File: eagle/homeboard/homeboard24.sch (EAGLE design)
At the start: 128 parts, among them IC1 XCF02S, IC2 25LC080SN, IC3 ATMEGA32U2-TQFP, Q5 BC848SMD, Q6 BC848SMD, Q7 BC848SMD, Q8 BC848SMD, T1 BSS138, T2 BC848, T3 BSS138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

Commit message: added text
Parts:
- removed C28, C30, C31: 100nF, rcl:C-EUC0603
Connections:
- net GND: no longer C28.2, C30.2, C31.2
- net VCC: no longer C28.1, C30.1, C31.1
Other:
- note added: "atmel"
- note added: "bot right"
- note added: "flash"
- note added: "prom"
- note added: "ram"
- moved on the sheet: C29, C32, C34

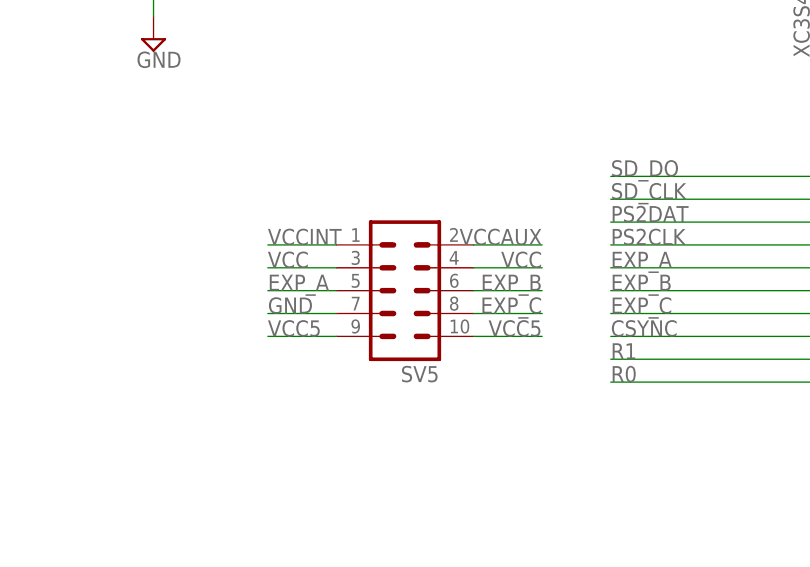
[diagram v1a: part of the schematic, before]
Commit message: moved ps2 stuff to top layer
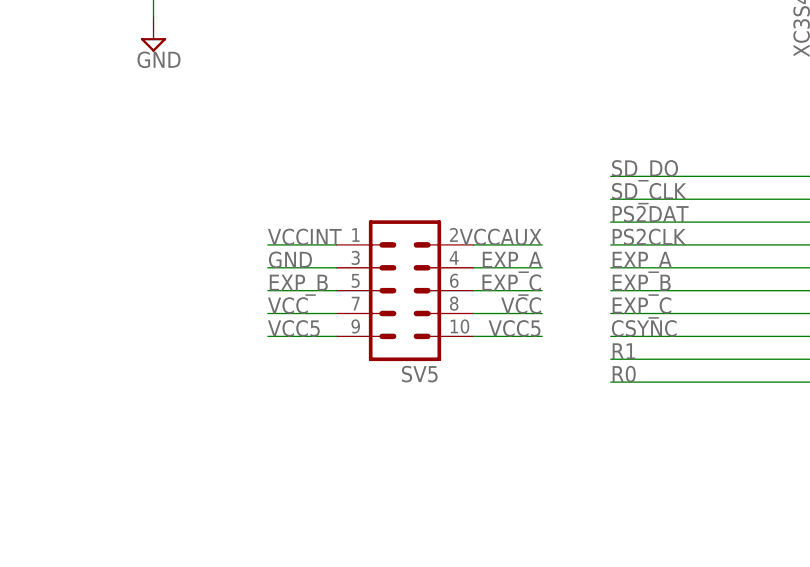
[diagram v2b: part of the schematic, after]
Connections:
- net EXP_A: now also SV5.4; no longer SV5.5
- net EXP_B: now also SV5.5; no longer SV5.6
- net EXP_C: now also SV5.6; no longer SV5.8
- net GND: now also SV5.3; no longer SV5.7
- net VCC: now also SV5.7, SV5.8; no longer SV5.3, SV5.4
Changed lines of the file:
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@@
-</segment>
-<segment>
-<pinref part="SV5" gate="G$1" pin="7"/>
-<wire x1="60.96" y1="-73.66" x2="68.58" y2="-73.66" width="0.1524" layer="91"/>
-<label x="60.96" y="-73.66" size="1.778" layer="95"/>
 </segment>
 <segment>
@@
 <pinref part="SV2" gate="1" pin="2"/>
 <wire x1="292.1" y1="-35.56" x2="292.1" y2="-25.4" width="0.1524" layer="91"/>
+</segment>
+<segment>
+<pinref part="SV5" gate="G$1" pin="3"/>
+<wire x1="60.96" y1="-68.58" x2="68.58" y2="-68.58" width="0.1524" layer="91"/>
+<label x="60.96" y="-68.58" size="1.778" layer="95"/>
 </segment>
 </net>
@@
 </segment>
 <segment>
-<pinref part="SV5" gate="G$1" pin="3"/>
-<wire x1="60.96" y1="-68.58" x2="68.58" y2="-68.58" width="0.1524" layer="91"/>
-<label x="60.96" y="-68.58" size="1.778" layer="95"/>
-</segment>
-<segment>
-<pinref part="SV5" gate="G$1" pin="4"/>
-<wire x1="91.44" y1="-68.58" x2="83.82" y2="-68.58" width="0.1524" layer="91"/>
-<label x="91.44" y="-68.58" size="1.778" layer="95" rot="MR0"/>
-</segment>
-<segment>
 <pinref part="R55" gate="G$1" pin="1"/>
 <pinref part="R56" gate="G$1" pin="1"/>
@@
 <junction x="287.02" y="-33.02"/>
 <label x="266.7" y="-33.02" size="1.778" layer="95"/>
+</segment>
+<segment>
+<pinref part="SV5" gate="G$1" pin="7"/>
+<wire x1="60.96" y1="-73.66" x2="68.58" y2="-73.66" width="0.1524" layer="91"/>
+<label x="60.96" y="-73.66" size="1.778" layer="95"/>
+</segment>
+<segment>
+<pinref part="SV5" gate="G$1" pin="8"/>
+<wire x1="91.44" y1="-73.66" x2="83.82" y2="-73.66" width="0.1524" layer="91"/>
+<label x="91.44" y="-73.66" size="1.778" layer="95" rot="MR0"/>
 </segment>
 </net>
@@
 </segment>
 <segment>
-<pinref part="SV5" gate="G$1" pin="5"/>
-<wire x1="60.96" y1="-71.12" x2="68.58" y2="-71.12" width="0.1524" layer="91"/>
-<label x="60.96" y="-71.12" size="1.778" layer="95"/>
+<pinref part="SV5" gate="G$1" pin="4"/>
+<wire x1="91.44" y1="-68.58" x2="83.82" y2="-68.58" width="0.1524" layer="91"/>
+<label x="91.44" y="-68.58" size="1.778" layer="95" rot="MR0"/>
 </segment>
 </net>
@@
 </segment>
 <segment>
-<pinref part="SV5" gate="G$1" pin="6"/>
-<wire x1="91.44" y1="-71.12" x2="83.82" y2="-71.12" width="0.1524" layer="91"/>
-<label x="91.44" y="-71.12" size="1.778" layer="95" rot="MR0"/>
+<pinref part="SV5" gate="G$1" pin="5"/>
+<wire x1="60.96" y1="-71.12" x2="68.58" y2="-71.12" width="0.1524" layer="91"/>
+<label x="60.96" y="-71.12" size="1.778" layer="95"/>
 </segment>
 </net>
@@
 </segment>
 <segment>
-<pinref part="SV5" gate="G$1" pin="8"/>
-<wire x1="91.44" y1="-73.66" x2="83.82" y2="-73.66" width="0.1524" layer="91"/>
-<label x="91.44" y="-73.66" size="1.778" layer="95" rot="MR0"/>
-</segment>
-</net>
+<pinref part="SV5" gate="G$1" pin="6"/>
+<wire x1="91.44" y1="-71.12" x2="83.82" y2="-71.12" width="0.1524" layer="91"/>
+<label x="91.44" y="-71.12" size="1.778" layer="95" rot="MR0"/>
+</segment>
+</net>

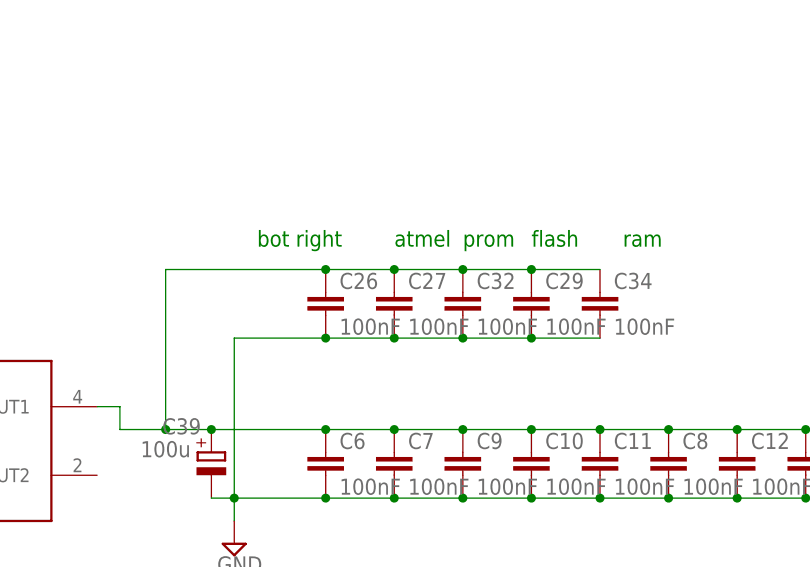
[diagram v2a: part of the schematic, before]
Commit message: removed spare cap
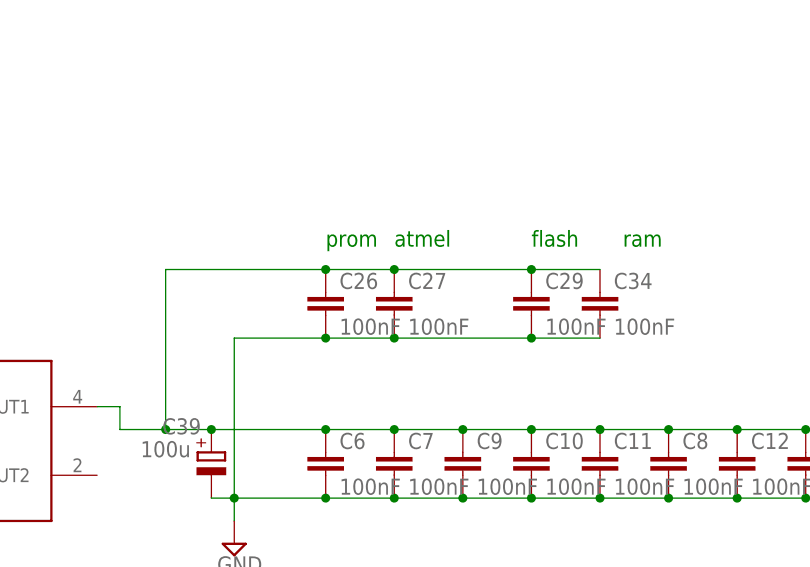
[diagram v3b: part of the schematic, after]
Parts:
- removed C32: 100nF, rcl:C-EUC0603
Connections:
- net GND: no longer C32.2
- net VCC: no longer C32.1
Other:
- note removed: "bot right"
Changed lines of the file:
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@@
 <part name="C27" library="rcl" deviceset="C-EU" device="C0603" value="100nF"/>
 <part name="C29" library="rcl" deviceset="C-EU" device="C0603" value="100nF"/>
-<part name="C32" library="rcl" deviceset="C-EU" device="C0603" value="100nF"/>
 <part name="X6" library="con-cypressindustries" deviceset="MINI-USB_4P-" device="85-32004-10X"/>
 <part name="R53" library="rcl" deviceset="R-EU_" device="R0805" value="22"/>
@@
 <text x="271.78" y="-254" size="1.778" layer="91">Possible alternative:</text>
 <text x="-139.7" y="132.08" size="1.778" layer="91">atmel</text>
-<text x="-154.94" y="132.08" size="1.778" layer="91">bot right</text>
-<text x="-132.08" y="132.08" size="1.778" layer="91">prom</text>
+<text x="-147.32" y="132.08" size="1.778" layer="91">prom</text>
 <text x="-124.46" y="132.08" size="1.778" layer="91">flash</text>
 <text x="-114.3" y="132.08" size="1.778" layer="91">ram</text>
@@
 <instance part="C27" gate="G$1" x="-139.7" y="127"/>
 <instance part="C29" gate="G$1" x="-124.46" y="127"/>
-<instance part="C32" gate="G$1" x="-132.08" y="127"/>
 <instance part="X6" gate="G$1" x="358.14" y="119.38" rot="MR0"/>
 <instance part="R53" gate="G$1" x="375.92" y="121.92" rot="MR180"/>
@@
 <junction x="-147.32" y="121.92"/>
 <junction x="-139.7" y="121.92"/>
-<pinref part="C32" gate="G$1" pin="2"/>
-<wire x1="-139.7" y1="121.92" x2="-132.08" y2="121.92" width="0.1524" layer="91"/>
 <pinref part="C29" gate="G$1" pin="2"/>
-<wire x1="-132.08" y1="121.92" x2="-124.46" y2="121.92" width="0.1524" layer="91"/>
-<junction x="-132.08" y="121.92"/>
+<wire x1="-139.7" y1="121.92" x2="-124.46" y2="121.92" width="0.1524" layer="91"/>
 <wire x1="-157.48" y1="121.92" x2="-157.48" y2="104.14" width="0.1524" layer="91"/>
 <junction x="-157.48" y="104.14"/>
@@
 <junction x="-147.32" y="129.54"/>
 <junction x="-139.7" y="129.54"/>
-<pinref part="C32" gate="G$1" pin="1"/>
-<wire x1="-139.7" y1="129.54" x2="-132.08" y2="129.54" width="0.1524" layer="91"/>
 <pinref part="C29" gate="G$1" pin="1"/>
-<wire x1="-132.08" y1="129.54" x2="-124.46" y2="129.54" width="0.1524" layer="91"/>
-<junction x="-132.08" y="129.54"/>
+<wire x1="-139.7" y1="129.54" x2="-124.46" y2="129.54" width="0.1524" layer="91"/>
 <pinref part="U$4" gate="G$1" pin="VOUT1"/>
 <wire x1="-172.72" y1="114.3" x2="-170.18" y2="114.3" width="0.1524" layer="91"/>

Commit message: moving around
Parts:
- removed SV4: (no value), con-lstb:MA10-2
- added SV1: (no value), con-lstb:MA10-2
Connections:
- net AT_RESET: now also SV1.2; no longer SV4.1
- net EMER_BOOT: now also SV1.1; no longer SV4.2
- net GND: now also SV1.5, SV1.6; no longer SV4.3, SV4.4
- net HDR_MISO: now also SV1.15; no longer SV4.13
- net HDR_MOSI: now also SV1.19; no longer SV4.17
- net HDR_SCLK: now also SV1.17; no longer SV4.15
- net HDR_SEL: now also SV1.13; no longer SV4.11
- net HDR_SPARE: now also SV1.11; no longer SV4.9
- net SPI_MISO: now also SV1.16; no longer SV4.14
- net SPI_MOSI: now also SV1.20; no longer SV4.18
- net SPI_SCLK: now also SV1.18; no longer SV4.16
- net SPI_SEL: now also SV1.14; no longer SV4.12
- net TCK: now also SV1.9; no longer SV4.7
- net TDI_FPGA: now also SV1.7; no longer SV4.5
- net TDO_EXP: now also SV1.8; no longer SV4.6
- net TDO_PROM: now also SV1.10; no longer SV4.8
- net TMS: now also SV1.12; no longer SV4.10
- net VCC: now also SV1.3, SV1.4; no longer SV4.19, SV4.20
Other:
- moved on the sheet: R55, R56
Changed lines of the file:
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@@
 <part name="U$9" library="cpcfpga" deviceset="GNDHOLE" device=""/>
 <part name="SV5" library="con-lstb" deviceset="MA05-2" device=""/>
-<part name="SV4" library="con-lstb" deviceset="MA10-2" device=""/>
 <part name="JP2" library="adafruit" deviceset="PINHD-1X3" device=""/>
 <part name="SV2" library="con-lstb" deviceset="MA03-2" device=""/>
 <part name="SUPPLY16" library="supply2" deviceset="GND" device=""/>
 <part name="C13" library="rcl" deviceset="C-EU" device="C0603" value="100nF"/>
+<part name="SV1" library="con-lstb" deviceset="MA10-2" device="">
+<attribute name="MF" value=""/>
+<attribute name="MPN" value=""/>
+<attribute name="OC_FARNELL" value="unknown"/>
+<attribute name="OC_NEWARK" value="unknown"/>
+</part>
 </parts>
 <sheets>
@@
 <instance part="C41" gate="G$1" x="378.46" y="114.3" rot="R270"/>
 <instance part="SUPPLY22" gate="GND" x="373.38" y="109.22"/>
-<instance part="R55" gate="G$1" x="312.42" y="45.72" rot="MR270"/>
-<instance part="R56" gate="G$1" x="289.56" y="45.72" rot="MR270"/>
+<instance part="R55" gate="G$1" x="292.1" y="48.26" rot="R270"/>
+<instance part="R56" gate="G$1" x="314.96" y="48.26" rot="R270"/>
 <instance part="U$3" gate="G$1" x="541.02" y="40.64"/>
 <instance part="C39" gate="G$1" x="-160.02" y="109.22" smashed="yes">
@@
 <instance part="U$9" gate="G$1" x="-73.66" y="137.16"/>
 <instance part="SV5" gate="G$1" x="76.2" y="-71.12" rot="R180"/>
-<instance part="SV4" gate="G$1" x="302.26" y="30.48" rot="R180"/>
 <instance part="JP2" gate="A" x="330.2" y="119.38" rot="R90"/>
 <instance part="SV2" gate="1" x="289.56" y="-17.78" rot="R90"/>
 <instance part="SUPPLY16" gate="GND" x="292.1" y="-38.1"/>
 <instance part="C13" gate="G$1" x="-93.98" y="109.22"/>
+<instance part="SV1" gate="G$1" x="302.26" y="33.02" rot="R180"/>
 </instances>
 <busses>
@@
 <wire x1="322.58" y1="38.1" x2="309.88" y2="38.1" width="0.1524" layer="91"/>
 <label x="322.58" y="38.1" size="1.778" layer="95" rot="MR0"/>
-<pinref part="SV4" gate="G$1" pin="4"/>
+<pinref part="SV1" gate="G$1" pin="6"/>
 </segment>
 <segment>
 <wire x1="294.64" y1="38.1" x2="281.94" y2="38.1" width="0.1524" layer="91"/>
 <label x="281.94" y="38.1" size="1.778" layer="95"/>
-<pinref part="SV4" gate="G$1" pin="3"/>
+<pinref part="SV1" gate="G$1" pin="5"/>
 </segment>
 <segment>
@@
 <pinref part="R55" gate="G$1" pin="1"/>
 <pinref part="R56" gate="G$1" pin="1"/>
-<wire x1="312.42" y1="50.8" x2="289.56" y2="50.8" width="0.1524" layer="91"/>
-<label x="299.72" y="50.8" size="1.778" layer="95"/>
-</segment>
-<segment>
-<pinref part="SV4" gate="G$1" pin="19"/>
+<wire x1="292.1" y1="53.34" x2="314.96" y2="53.34" width="0.1524" layer="91"/>
+<label x="304.8" y="53.34" size="1.778" layer="95" rot="MR0"/>
+<pinref part="SV1" gate="G$1" pin="3"/>
+<wire x1="294.64" y1="40.64" x2="327.66" y2="40.64" width="0.1524" layer="91"/>
+<wire x1="327.66" y1="40.64" x2="327.66" y2="53.34" width="0.1524" layer="91"/>
+<wire x1="327.66" y1="53.34" x2="314.96" y2="53.34" width="0.1524" layer="91"/>
+<junction x="314.96" y="53.34"/>
+<pinref part="SV1" gate="G$1" pin="4"/>
+<wire x1="309.88" y1="40.64" x2="276.86" y2="40.64" width="0.1524" layer="91"/>
+<wire x1="276.86" y1="40.64" x2="276.86" y2="53.34" width="0.1524" layer="91"/>
+<wire x1="276.86" y1="53.34" x2="292.1" y2="53.34" width="0.1524" layer="91"/>
+<junction x="292.1" y="53.34"/>
+</segment>
+<segment>
 <wire x1="281.94" y1="17.78" x2="294.64" y2="17.78" width="0.1524" layer="91"/>
 <label x="281.94" y="17.78" size="1.778" layer="95"/>
 </segment>
 <segment>
-<pinref part="SV4" gate="G$1" pin="20"/>
 <wire x1="322.58" y1="17.78" x2="309.88" y2="17.78" width="0.1524" layer="91"/>
 <label x="322.58" y="17.78" size="1.778" layer="95" rot="MR0"/>
@@
 <wire x1="281.94" y1="33.02" x2="294.64" y2="33.02" width="0.1524" layer="91"/>
 <label x="281.94" y="33.02" size="1.778" layer="95"/>
-<pinref part="SV4" gate="G$1" pin="7"/>
+<pinref part="SV1" gate="G$1" pin="9"/>
 </segment>
 <segment>
@@
 <label x="322.58" y="30.48" size="1.778" layer="95" rot="MR0"/>
 <wire x1="322.58" y1="30.48" x2="309.88" y2="30.48" width="0.1524" layer="91"/>
-<pinref part="SV4" gate="G$1" pin="10"/>
+<pinref part="SV1" gate="G$1" pin="12"/>
 </segment>
 </net>
@@
 <wire x1="281.94" y1="35.56" x2="294.64" y2="35.56" width="0.1524" layer="91"/>
 <label x="281.94" y="35.56" size="1.778" layer="95"/>
-<pinref part="SV4" gate="G$1" pin="5"/>
+<pinref part="SV1" gate="G$1" pin="7"/>
 </segment>
 </net>
@@
 <segment>
 <wire x1="322.58" y1="22.86" x2="309.88" y2="22.86" width="0.1524" layer="91"/>
-<pinref part="SV4" gate="G$1" pin="16"/>
 <label x="322.58" y="22.86" size="1.778" layer="95" rot="MR0"/>
+<pinref part="SV1" gate="G$1" pin="18"/>
 </segment>
 </net>
@@
 </segment>
 <segment>
-<pinref part="SV4" gate="G$1" pin="18"/>
 <wire x1="322.58" y1="20.32" x2="309.88" y2="20.32" width="0.1524" layer="91"/>
 <label x="322.58" y="20.32" size="1.778" layer="95" rot="MR0"/>
+<pinref part="SV1" gate="G$1" pin="20"/>
 </segment>
 </net>
@@
 </segment>
 <segment>
-<pinref part="SV4" gate="G$1" pin="14"/>
 <wire x1="322.58" y1="25.4" x2="309.88" y2="25.4" width="0.1524" layer="91"/>
 <label x="322.58" y="25.4" size="1.778" layer="95" rot="MR0"/>
+<pinref part="SV1" gate="G$1" pin="16"/>
 </segment>
 </net>
@@
 <wire x1="322.58" y1="27.94" x2="309.88" y2="27.94" width="0.1524" layer="91"/>
 <label x="322.58" y="27.94" size="1.778" layer="95" rot="MR0"/>
-<pinref part="SV4" gate="G$1" pin="12"/>
+<pinref part="SV1" gate="G$1" pin="14"/>
 </segment>
 </net>
@@
 </segment>
 <segment>
-<wire x1="322.58" y1="40.64" x2="312.42" y2="40.64" width="0.1524" layer="91"/>
-<label x="322.58" y="40.64" size="1.778" layer="95" rot="MR0"/>
+<wire x1="281.94" y1="43.18" x2="292.1" y2="43.18" width="0.1524" layer="91"/>
+<label x="281.94" y="43.18" size="1.778" layer="95"/>
 <pinref part="R55" gate="G$1" pin="2"/>
-<wire x1="312.42" y1="40.64" x2="309.88" y2="40.64" width="0.1524" layer="91"/>
-<junction x="312.42" y="40.64"/>
-<pinref part="SV4" gate="G$1" pin="2"/>
+<pinref part="SV1" gate="G$1" pin="1"/>
+<wire x1="292.1" y1="43.18" x2="294.64" y2="43.18" width="0.1524" layer="91"/>
+<junction x="292.1" y="43.18"/>
 </segment>
 </net>
@@
 <wire x1="322.58" y1="33.02" x2="309.88" y2="33.02" width="0.1524" layer="91"/>
 <label x="322.58" y="33.02" size="1.778" layer="95" rot="MR0"/>
-<pinref part="SV4" gate="G$1" pin="8"/>
+<pinref part="SV1" gate="G$1" pin="10"/>
 </segment>
 </net>
@@
 <wire x1="322.58" y1="35.56" x2="309.88" y2="35.56" width="0.1524" layer="91"/>
 <label x="322.58" y="35.56" size="1.778" layer="95" rot="MR0"/>
-<pinref part="SV4" gate="G$1" pin="6"/>
+<pinref part="SV1" gate="G$1" pin="8"/>
 </segment>
 </net>
@@
 </segment>
 <segment>
-<wire x1="281.94" y1="40.64" x2="289.56" y2="40.64" width="0.1524" layer="91"/>
-<label x="281.94" y="40.64" size="1.778" layer="95"/>
+<wire x1="322.58" y1="43.18" x2="314.96" y2="43.18" width="0.1524" layer="91"/>
+<label x="322.58" y="43.18" size="1.778" layer="95" rot="MR0"/>
 <pinref part="R56" gate="G$1" pin="2"/>
-<wire x1="289.56" y1="40.64" x2="294.64" y2="40.64" width="0.1524" layer="91"/>
-<junction x="289.56" y="40.64"/>
-<pinref part="SV4" gate="G$1" pin="1"/>
+<pinref part="SV1" gate="G$1" pin="2"/>
+<wire x1="309.88" y1="43.18" x2="314.96" y2="43.18" width="0.1524" layer="91"/>
+<junction x="314.96" y="43.18"/>
 </segment>
 </net>
@@
 <net name="HDR_MOSI" class="0">
 <segment>
-<pinref part="SV4" gate="G$1" pin="17"/>
 <wire x1="281.94" y1="20.32" x2="294.64" y2="20.32" width="0.1524" layer="91"/>
 <label x="281.94" y="20.32" size="1.778" layer="95"/>
+<pinref part="SV1" gate="G$1" pin="19"/>
 </segment>
 <segment>
@@
 <net name="HDR_SCLK" class="0">
 <segment>
-<pinref part="SV4" gate="G$1" pin="15"/>
 <wire x1="294.64" y1="22.86" x2="281.94" y2="22.86" width="0.1524" layer="91"/>
 <label x="281.94" y="22.86" size="1.778" layer="95"/>
+<pinref part="SV1" gate="G$1" pin="17"/>
 </segment>
 <segment>
@@
 <net name="HDR_MISO" class="0">
 <segment>
-<pinref part="SV4" gate="G$1" pin="13"/>
 <wire x1="281.94" y1="25.4" x2="294.64" y2="25.4" width="0.1524" layer="91"/>
 <label x="281.94" y="25.4" size="1.778" layer="95"/>
+<pinref part="SV1" gate="G$1" pin="15"/>
 </segment>
 <segment>
@@
 <wire x1="281.94" y1="27.94" x2="294.64" y2="27.94" width="0.1524" layer="91"/>
 <label x="281.94" y="27.94" size="1.778" layer="95"/>
-<pinref part="SV4" gate="G$1" pin="11"/>
+<pinref part="SV1" gate="G$1" pin="13"/>
 </segment>
 <segment>
@@
 <wire x1="281.94" y1="30.48" x2="294.64" y2="30.48" width="0.1524" layer="91"/>
 <label x="281.94" y="30.48" size="1.778" layer="95"/>
-<pinref part="SV4" gate="G$1" pin="9"/>
-</segment>
-<segment>
+<pinref part="SV1" gate="G$1" pin="11"/>
+</segment>
+<segment>
